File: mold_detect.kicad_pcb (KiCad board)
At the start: 2 copper layers, 57 x 57 mm, 46 parts, among them J1 USB_C_Receptacle_USB2.0_14P, J2 ISP, U1 TPL5010, U2 FT230XS, U3 ATmega328P-P, U4 SHT30-DIS, U5 W25Q128JVS, Y1 16MHz

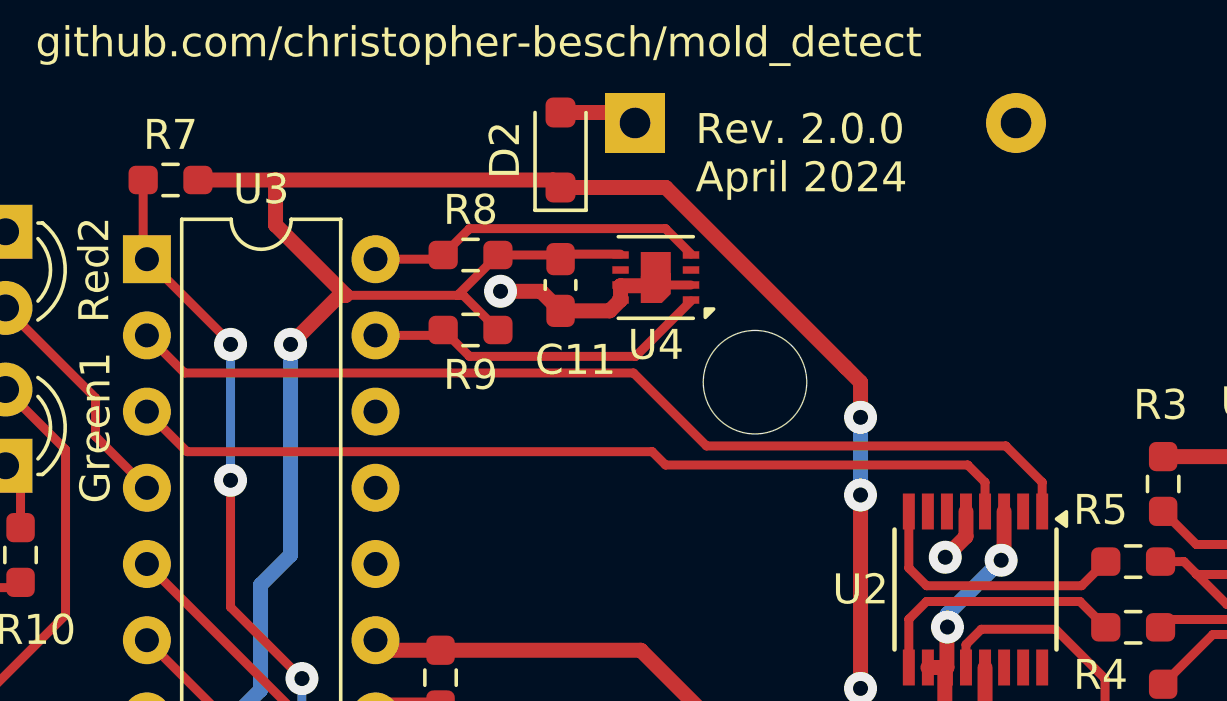
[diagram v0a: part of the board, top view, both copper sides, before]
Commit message: added battery holder to 3d print
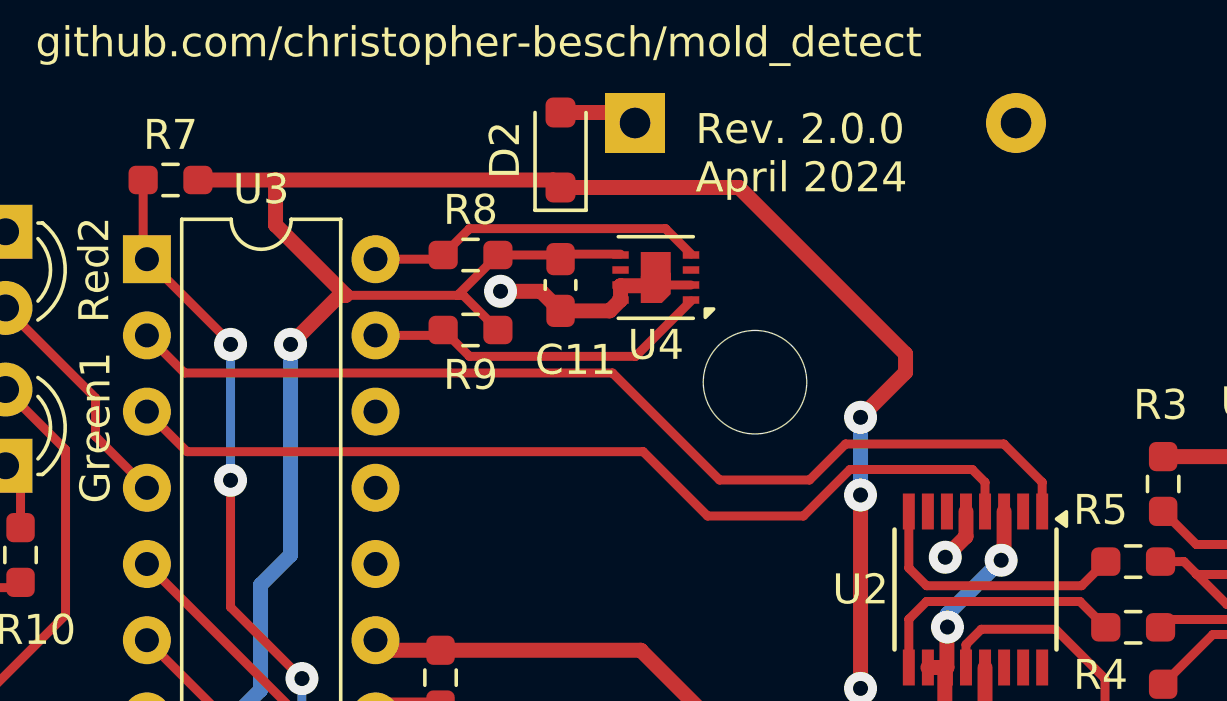
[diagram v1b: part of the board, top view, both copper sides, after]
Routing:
- net +3V0: track 135.4 -> 138.1 mm
- net TXD: track 29.9 -> 31.2 mm
- net RXD: track 32.8 -> 33.8 mm
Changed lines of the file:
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@@
+	)
+	(segment
+		(start 74.5 53.25)
+		(end 80.45 53.25)
+		(width 0.5)
+		(layer "F.Cu")
+		(net 5)
 	)
 	(segment
@@
 	)
 	(segment
+		(start 80.45 53.25)
+		(end 86 58.8)
+		(width 0.5)
+		(layer "F.Cu")
+		(net 5)
+	)
+	(segment
 		(start 62 91.5)
 		(end 59.5 94)
@@
 	)
 	(segment
+		(start 86 59.411)
+		(end 84.5 60.911)
+		(width 0.5)
+		(layer "F.Cu")
+		(net 5)
+	)
+	(segment
 		(start 65 53)
 		(end 62.4125 53)
@@
 	)
 	(segment
-		(start 84 59.242)
-		(end 84.5 59.742)
-		(width 0.5)
-		(layer "F.Cu")
-		(net 5)
-	)
-	(segment
-		(start 74.5 53.25)
-		(end 78.008 53.25)
-		(width 0.5)
-		(layer "F.Cu")
-		(net 5)
-	)
-	(segment
-		(start 78.008 53.25)
-		(end 84 59.242)
-		(width 0.5)
-		(layer "F.Cu")
-		(net 5)
-	)
-	(segment
 		(start 67.344 56.844)
 		(end 67.135 56.844)
@@
 	)
 	(segment
-		(start 84.5 59.742)
-		(end 84.5 60.911)
-		(width 0.5)
-		(layer "F.Cu")
-		(net 5)
-	)
-	(segment
 		(start 74.25 53)
 		(end 65 53)
@@
 	)
 	(segment
+		(start 86 58.8)
+		(end 86 59.411)
+		(width 0.5)
+		(layer "F.Cu")
+		(net 5)
+	)
+	(segment
 		(start 80.4125 72.5)
 		(end 79.3625 73.55)
@@
 	)
 	(segment
-		(start 89.343 61.865)
-		(end 90.555 63.077)
+		(start 61.9655 59.433)
+		(end 76.233 59.433)
 		(width 0.3)
 		(layer "F.Cu")
@@
 	)
 	(segment
-		(start 61.9655 59.433)
-		(end 76.933 59.433)
-		(width 0.3)
-		(layer "F.Cu")
-		(net 13)
-	)
-	(segment
-		(start 79.365 61.865)
-		(end 89.343 61.865)
+		(start 82.8 63)
+		(end 84 61.8)
 		(width 0.3)
 		(layer "F.Cu")
@@
 	)
 	(segment
-		(start 76.933 59.433)
-		(end 79.365 61.865)
+		(start 79.8 63)
+		(end 82.8 63)
+		(width 0.3)
+		(layer "F.Cu")
+		(net 13)
+	)
+	(segment
+		(start 89.278 61.8)
+		(end 90.555 63.077)
+		(width 0.3)
+		(layer "F.Cu")
+		(net 13)
+	)
+	(segment
+		(start 84 61.8)
+		(end 89.278 61.8)
+		(width 0.3)
+		(layer "F.Cu")
+		(net 13)
+	)
+	(segment
+		(start 76.233 59.433)
+		(end 79.8 63)
 		(width 0.3)
 		(layer "F.Cu")
@@
 	)
 	(segment
-		(start 78 62.5)
-		(end 88.073 62.5)
-		(width 0.3)
-		(layer "F.Cu")
-		(net 15)
-	)
-	(segment
 		(start 60.7125 60.72)
 		(end 62.0485 62.056)
@@
 	)
 	(segment
-		(start 88.073 62.5)
+		(start 82.597918 64.2)
+		(end 84.147918 62.65)
+		(width 0.3)
+		(layer "F.Cu")
+		(net 15)
+	)
+	(segment
+		(start 77.256 62.056)
+		(end 79.4 64.2)
+		(width 0.3)
+		(layer "F.Cu")
+		(net 15)
+	)
+	(segment
+		(start 84.147918 62.65)
+		(end 88.223 62.65)
+		(width 0.3)
+		(layer "F.Cu")
+		(net 15)
+	)
+	(segment
+		(start 79.4 64.2)
+		(end 82.597918 64.2)
+		(width 0.3)
+		(layer "F.Cu")
+		(net 15)
+	)
+	(segment
+		(start 88.223 62.65)
 		(end 88.65 63.077)
 		(width 0.3)
@@
 	(segment
 		(start 62.0485 62.056)
-		(end 77.556 62.056)
-		(width 0.3)
-		(layer "F.Cu")
-		(net 15)
-	)
-	(segment
-		(start 77.556 62.056)
-		(end 78 62.5)
-		(width 0.3)
-		(layer "F.Cu")
+		(end 77.256 62.056)
+		(width 0.3)
+		(layer "F.Cu")

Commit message: before removing gnd connections
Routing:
- net RST: track 82.8 -> 89.7 mm, vias 4 -> 2
